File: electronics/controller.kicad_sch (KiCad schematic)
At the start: 13 parts, among them J2 UART GND TX RX, J3 RESET, U1 Pico H socketed

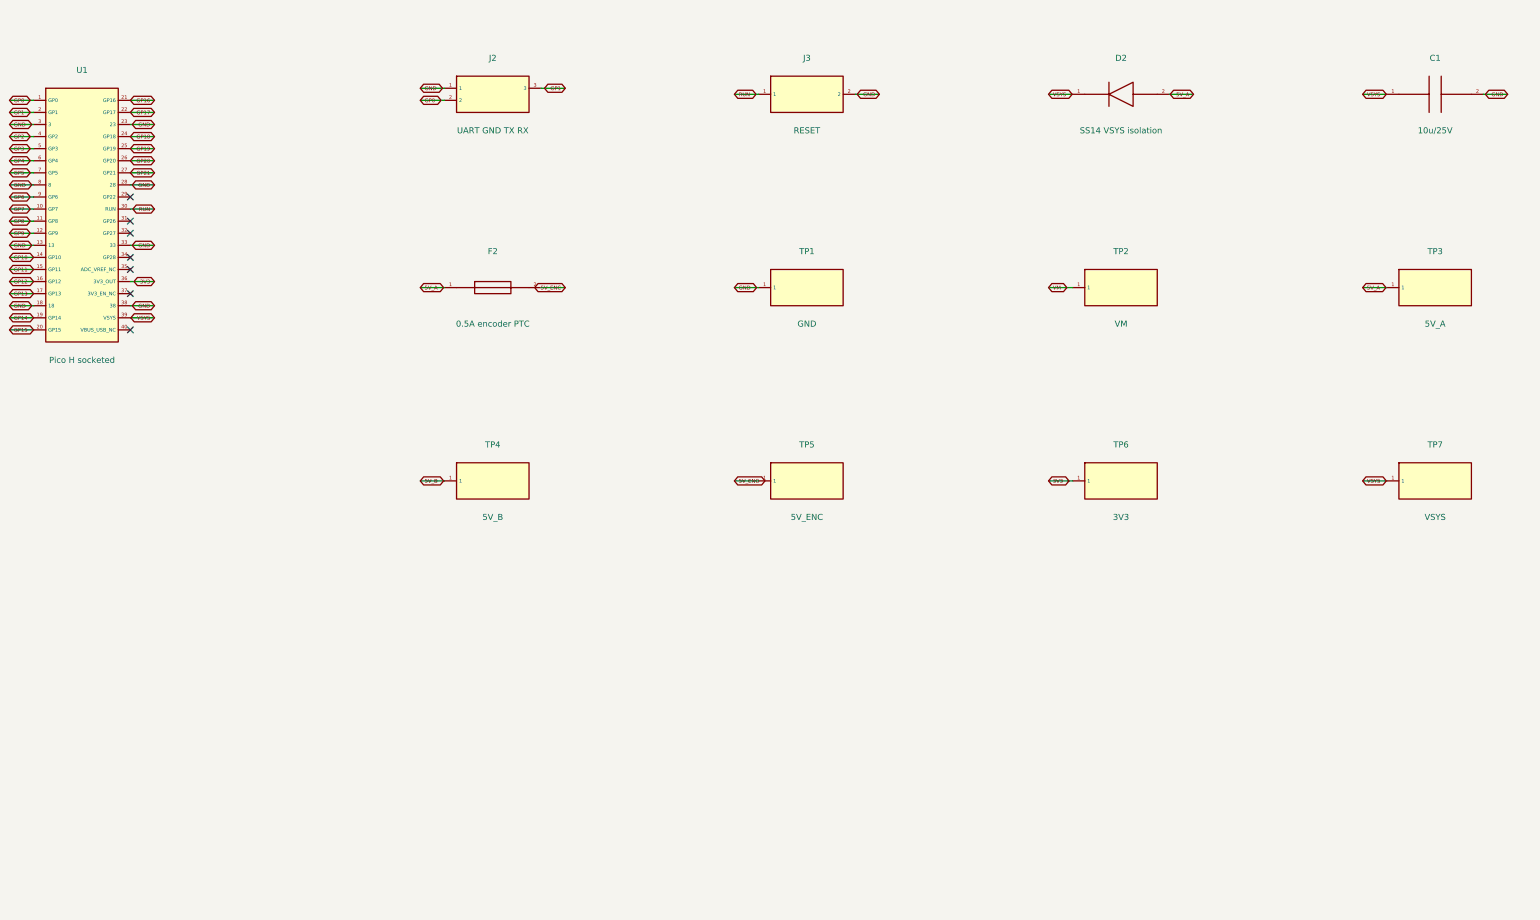
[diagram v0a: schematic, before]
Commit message: Integrate onboard RP2040 and drawing-based EV3 jacks on A1 PCB
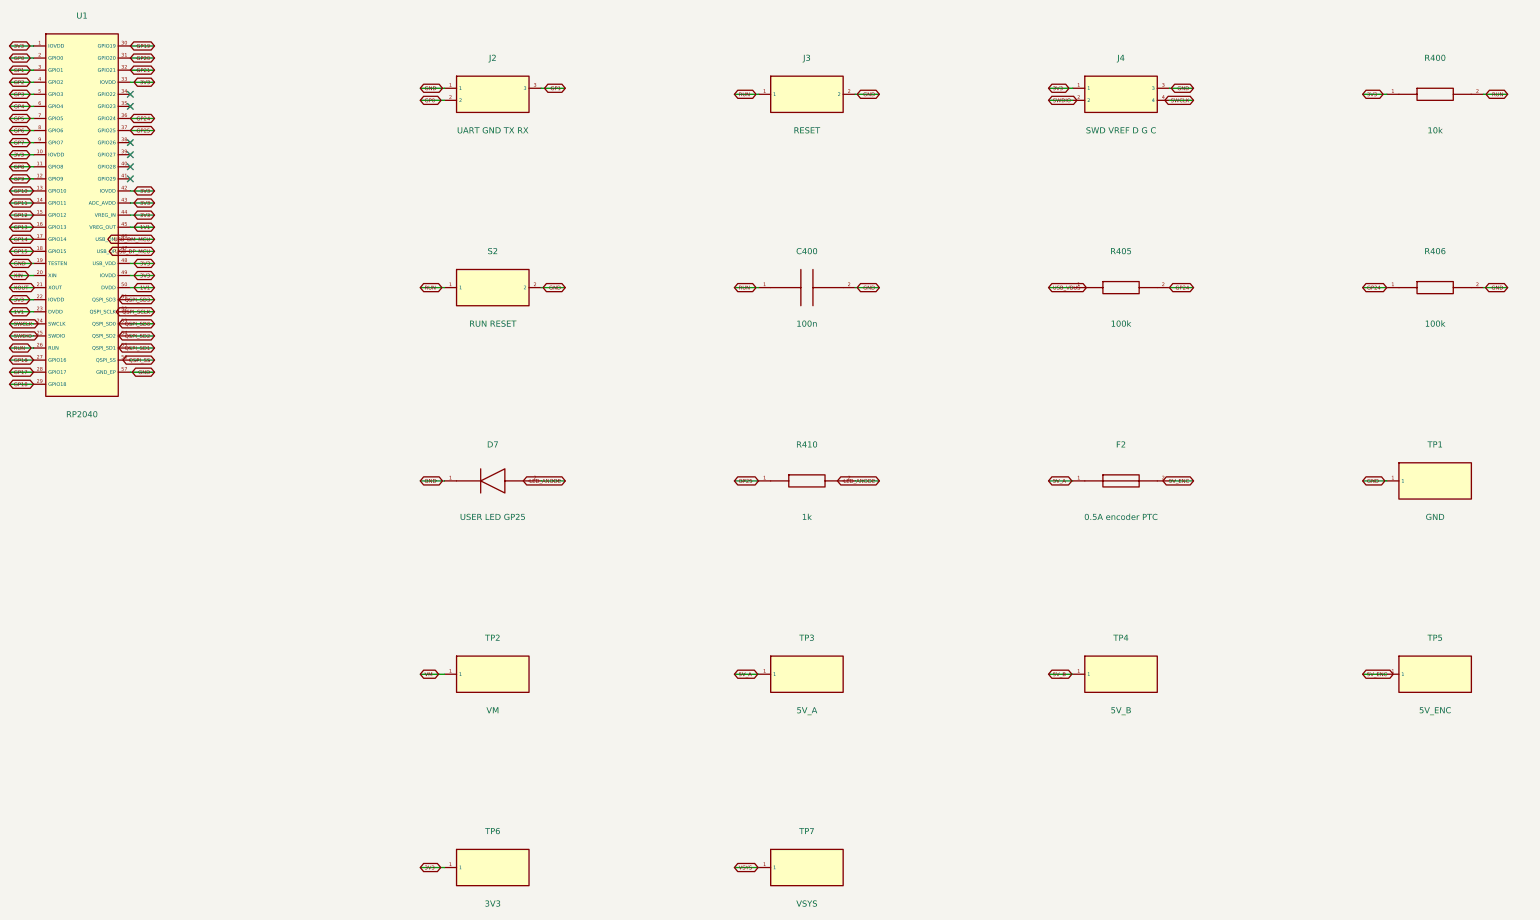
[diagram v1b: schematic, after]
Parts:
- removed C1: 10u/25V, Quadcuber:C_1210_3225Metric, symbol Quadcuber:C1
- removed D2: SS14 VSYS isolation, Quadcuber:D_SMA, symbol Quadcuber:D2
- added C400: 100n, Quadcuber:C_0402_1005Metric, symbol Quadcuber:C400
- added D7: USER LED GP25, Quadcuber:LED_0603_1608Metric, symbol Quadcuber:D7
- added J4: SWD VREF D G C, Quadcuber:PinHeader_1x04_P2.54mm_Vertical, symbol Quadcuber:J4
- added R400: 10k, Quadcuber:R_0603_1608Metric, symbol Quadcuber:R400
- added R405: 100k, Quadcuber:R_0603_1608Metric, symbol Quadcuber:R405
- added R406: 100k, Quadcuber:R_0603_1608Metric, symbol Quadcuber:R406
- added R410: 1k, Quadcuber:R_0603_1608Metric, symbol Quadcuber:R410
- added S2: RUN RESET, Quadcuber:SW_SPST_TL3342, symbol Quadcuber:S2
- TP1, TP2, TP3, TP4, TP5, TP6, TP7: now left out of the parts list
- U1: value Pico H socketed -> RP2040; footprint Quadcuber:Pico_H_Sockets -> Quadcuber:QFN-56-1EP_7x7mm_P0.4mm_EP3.2x3.2mm_ThermalVias; MPN SC0917 -> RP2040
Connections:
- net 3V3: now also U1.1 (IOVDD), U1.10 (IOVDD), U1.22 (IOVDD), U1.33 (IOVDD), U1.42 (IOVDD), U1.43 (ADC_AVDD), U1.44 (VREG_IN), U1.48 (USB_VDD), U1.49 (IOVDD), J4.1, R400.1; no longer U1.36 (3V3_OUT)
- net GND: now also U1.19 (TESTEN), U1.57 (GND_EP), C400.2, D7.1 (K), J4.3, R406.2, S2.2; no longer U1.13, U1.18, U1.23, U1.28, U1.3, U1.33, U1.38, U1.8
- net GP0: now also U1.2 (GPIO0); no longer U1.1 (GP0)
- net GP1: now also U1.3 (GPIO1); no longer U1.2 (GP1)
- net GP10: now also U1.13 (GPIO10); no longer U1.14 (GP10)
- net GP11: now also U1.14 (GPIO11); no longer U1.15 (GP11)
- net GP12: now also U1.15 (GPIO12); no longer U1.16 (GP12)
- net GP13: now also U1.16 (GPIO13); no longer U1.17 (GP13)
- net GP14: now also U1.17 (GPIO14); no longer U1.19 (GP14)
- net GP15: now also U1.18 (GPIO15); no longer U1.20 (GP15)
- net GP16: now also U1.27 (GPIO16); no longer U1.21 (GP16)
- net GP17: now also U1.28 (GPIO17); no longer U1.22 (GP17)
- net GP18: now also U1.29 (GPIO18); no longer U1.24 (GP18)
- net GP19: now also U1.30 (GPIO19); no longer U1.25 (GP19)
- net GP20: now also U1.31 (GPIO20); no longer U1.26 (GP20)
- net GP21: now also U1.32 (GPIO21); no longer U1.27 (GP21)
- net GP6: now also U1.8 (GPIO6); no longer U1.9 (GP6)
- net GP7: now also U1.9 (GPIO7); no longer U1.10 (GP7)
- net RUN: now also U1.26 (RUN), C400.1, R400.2, S2.1; no longer U1.30 (RUN)
- net VSYS: no longer U1.39 (VSYS)
- net GP25: now reaches U1.37 (GPIO25)
- net GP25: now also R410.1
- new net 1V1: U1.23 (DVDD), U1.45 (VREG_OUT), U1.50 (DVDD)
- new net GP24: R405.2, R406.1, U1.36 (GPIO24)
- new net LED_ANODE: D7.2 (A), R410.2
- new net QSPI_SCLK: U1.52 (QSPI_SCLK)
- new net QSPI_SD0: U1.53 (QSPI_SD0)
- new net QSPI_SD1: U1.55 (QSPI_SD1)
- new net QSPI_SD2: U1.54 (QSPI_SD2)
- new net QSPI_SD3: U1.51 (QSPI_SD3)
- new net QSPI_SS: U1.56 (QSPI_SS)
- new net SWCLK: J4.4, U1.24 (SWCLK)
- new net SWDIO: J4.2, U1.25 (SWDIO)
- new net USB_DM_MCU: U1.46 (USB_DM)
- new net USB_DP_MCU: U1.47 (USB_DP)
- new net USB_VBUS: R405.1
- new net XIN: U1.20 (XIN)
- new net XOUT: U1.21 (XOUT)
- no-connect marks 7 -> 6
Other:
- title: Quadcuber A0 / controller / ENGINEERING HOLD -> Quadcuber A1 / controller / ENGINEERING HOLD
- moved on the sheet: F2, TP1, TP2, TP3, TP4, TP5, TP6, TP7

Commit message: Migrate A1 to KiCad 10 and record blocked vendor-model transients
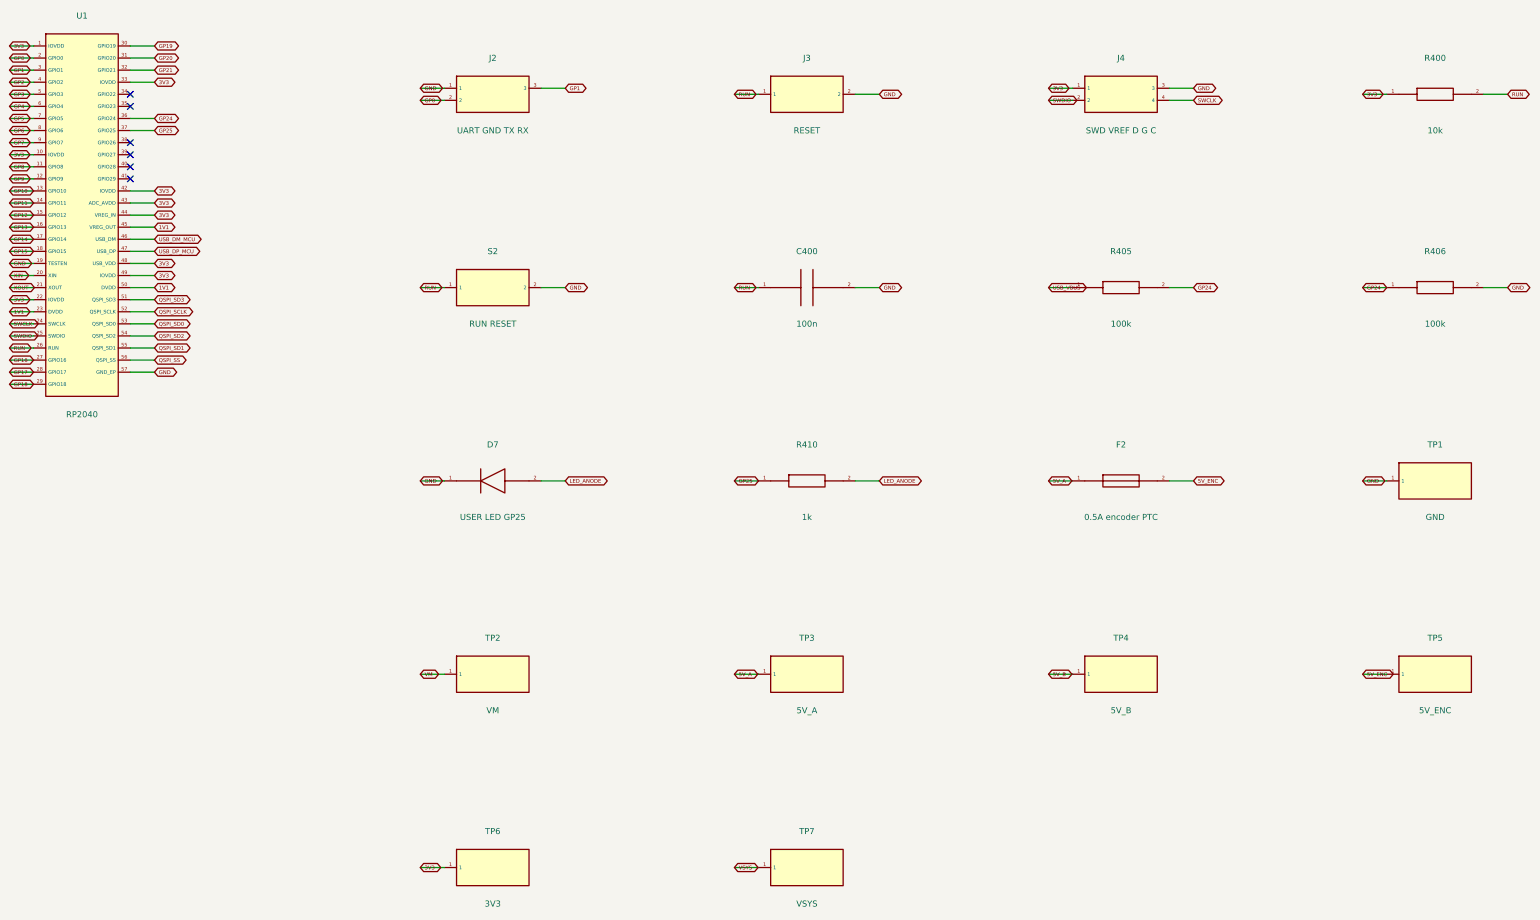
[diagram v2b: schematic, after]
